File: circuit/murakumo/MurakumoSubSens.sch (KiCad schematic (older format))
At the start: 2 parts

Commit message: hoge
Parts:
- removed U?: S7136, symbol S7136:S7136
- added C35, C36: 0.1u, symbol Device:C
- added D20, D21: LED, symbol Device:LED
- added D22, D23: SIR19-21C/TR8, symbol Device:LED
- added J16, J17: Conn_01x03, symbol Connector_Generic:Conn_01x03
- added R49, R50, R51, R52: R, symbol Device:R
- added R53, R54: 10k, symbol Device:R
- added U6: S7136, symbol S7136:S7136
- gave numbers to parts that had none: 1
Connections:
- net at U5.1 (Cathode): now also D22.1 (K)
- net +5V: now reaches U5.2 (VCC)
- net +5V: now also C35.1, C36.1, J16.3 (Pin_3), J17.3 (Pin_3), R49.1, R50.1, R51.1, R52.1, R53.1, R54.1, U6.2 (VCC)
- net at U5.3 (VOUT): now also D20.1 (K), J16.2 (Pin_2), R53.2
- net GND: now reaches U5.4 (GND)
- net GND: now also C35.2, C36.2, J16.1 (Pin_1), J17.1 (Pin_1), U6.4 (GND)
- new net: D22.2 (A), R51.2
- new net: D20.2 (A), R49.2
- new net: D23.1 (K), U6.1 (Cathode)
- new net: D21.1 (K), J17.2 (Pin_2), R54.2, U6.3 (VOUT)
- new net: D23.2 (A), R52.2
- new net: D21.2 (A), R50.2

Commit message: hoge
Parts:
- removed C35: 0.1u, symbol Device:C
- removed D20, D21: LED, symbol Device:LED
- removed D22: SIR19-21C/TR8, symbol Device:LED
- removed J16: Conn_01x03, symbol Connector_Generic:Conn_01x03
- removed R49, R50, R51: R, symbol Device:R
- removed R53, R54: 10k, symbol Device:R
- removed U5: S7136, symbol S7136:S7136
- added C?: 0.1u, symbol Device:C
- added D?: SIR19-21C/TR8, symbol Device:LED
- added J?: Conn_01x03, symbol Connector_Generic:Conn_01x03
- added R?: 68, symbol Device:R
- added U?: S7136, symbol S7136:S7136
- R52: value R -> 68
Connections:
- net +5V: now also C?.1, J?.3 (Pin_3), R?.1, U?.2 (VCC)
- net GND: now also C?.2, J?.1 (Pin_1), U?.4 (GND)
- new net: D?.1 (K), U?.1 (Cathode)
- new net: J?.2 (Pin_2), U?.3 (VOUT)
- new net: D?.2 (A), R?.2
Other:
- moved on the sheet: C36, J17

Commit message: オシレータ増やした。モータドライバの信号を CPU で読めるようにした。nRST にプルアップ抵抗を接続。まだ CPU の正しいピンに正しい線をつなげることができていない。
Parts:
- gave numbers to parts that had none: 5
- renumbered C36 to C47, D23 to D25, J17 to J20, R52 to R59, U6 to U9
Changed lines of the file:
@@
 $EndDescr
 $Comp
-L S7136:S7136 U6
+L S7136:S7136 U9
 U 1 1 61F63F2D
 P 7000 3450
-F 0 "U6" H 7000 3765 50  0000 C CNN
+F 0 "U9" H 7000 3765 50  0000 C CNN
 F 1 "S7136" H 7000 3674 50  0000 C CNN
 F 2 "" H 7000 3450 50  0001 C CNN
@@
 	7450 3400 7550 3400
 $Comp
-L Device:LED D23
+L Device:LED D25
 U 1 1 61F63F34
 P 7700 3200
-F 0 "D23" V 7739 3082 50  0000 R CNN
+F 0 "D25" V 7739 3082 50  0000 R CNN
 F 1 "SIR19-21C/TR8" V 7648 3082 50  0000 R CNN
 F 2 "" H 7700 3200 50  0001 C CNN
@@
 $EndComp
 $Comp
-L Device:R R52
+L Device:R R59
 U 1 1 61F63F3A
 P 7700 2800
-F 0 "R52" H 7770 2846 50  0000 L CNN
+F 0 "R59" H 7770 2846 50  0000 L CNN
 F 1 "68" H 7770 2755 50  0000 L CNN
 F 2 "" V 7630 2800 50  0001 C CNN
@@
 	7550 2500 7700 2500
 $Comp
-L Connector_Generic:Conn_01x03 J17
+L Connector_Generic:Conn_01x03 J20
 U 1 1 61F63F62
 P 5950 3400
-F 0 "J17" H 5868 3075 50  0000 C CNN
+F 0 "J20" H 5868 3075 50  0000 C CNN
 F 1 "Conn_01x03" H 5868 3166 50  0000 C CNN
 F 2 "" H 5950 3400 50  0001 C CNN
@@
 Connection ~ 6300 2500
 $Comp
-L Device:C C36
+L Device:C C47
 U 1 1 61F63F73
 P 6450 2950
-F 0 "C36" H 6565 2996 50  0000 L CNN
+F 0 "C47" H 6565 2996 50  0000 L CNN
 F 1 "0.1u" H 6565 2905 50  0000 L CNN
 F 2 "" H 6488 2800 50  0001 C CNN
@@
 Connection ~ 6450 2500
 $Comp
-L power:GND #PWR0242
+L power:GND #PWR0164
 U 1 1 61F6B876
 P 6450 3600
-F 0 "#PWR0242" H 6450 3350 50  0001 C CNN
+F 0 "#PWR0164" H 6450 3350 50  0001 C CNN
 F 1 "GND" H 6455 3427 50  0000 C CNN
 F 2 "" H 6450 3600 50  0001 C CNN
@@
 	6450 3600 6450 3500
 $Comp
-L power:PWR_FLAG #FLG0106
-U 1 1 61F6D0AF
-P 6250 4200
-F 0 "#FLG0106" H 6250 4275 50  0001 C CNN
-F 1 "PWR_FLAG" H 6250 4373 50  0000 C CNN
-F 2 "" H 6250 4200 50  0001 C CNN
-F 3 "~" H 6250 4200 50  0001 C CNN
-	1    6250 4200
-	1    0    0    -1
-$EndComp
-$Comp
-L power:GND #PWR0243
-U 1 1 61F6D38D
-P 6250 4450
-F 0 "#PWR0243" H 6250 4200 50  0001 C CNN
-F 1 "GND" H 6255 4277 50  0000 C CNN
-F 2 "" H 6250 4450 50  0001 C CNN
-F 3 "" H 6250 4450 50  0001 C CNN
-	1    6250 4450
-	1    0    0    -1
-$EndComp
-Wire Wire Line
-	6250 4450 6250 4200
-$Comp
-L power:PWR_FLAG #FLG0107
-U 1 1 61F6EBC2
-P 5750 4450
-F 0 "#FLG0107" H 5750 4525 50  0001 C CNN
-F 1 "PWR_FLAG" H 5750 4623 50  0000 C CNN
-F 2 "" H 5750 4450 50  0001 C CNN
-F 3 "~" H 5750 4450 50  0001 C CNN
-	1    5750 4450
-	-1   0    0    1
-$EndComp
-Wire Wire Line
-	5750 4450 5750 4200
-$Comp
-L power:+5V #PWR0240
+L power:+5V #PWR0162
 U 1 1 624AE95B
 P 6300 2400
-F 0 "#PWR0240" H 6300 2250 50  0001 C CNN
+F 0 "#PWR0162" H 6300 2250 50  0001 C CNN
 F 1 "+5V" H 6315 2573 50  0000 C CNN
 F 2 "" H 6300 2400 50  0001 C CNN
@@
 	1    0    0    -1
 $EndComp
-$Comp
-L power:+5V #PWR0244
-U 1 1 624AF64C
-P 5750 4200
-F 0 "#PWR0244" H 5750 4050 50  0001 C CNN
-F 1 "+5V" H 5765 4373 50  0000 C CNN
-F 2 "" H 5750 4200 50  0001 C CNN
-F 3 "" H 5750 4200 50  0001 C CNN
-	1    5750 4200
-	1    0    0    -1
-$EndComp
 Wire Wire Line
 	6450 2500 7550 2500
@@
 	6150 3400 6550 3400
 $Comp
-L S7136:S7136 U?
+L S7136:S7136 U8
 U 1 1 62E812F5
 P 4300 3450
-F 0 "U?" H 4300 3765 50  0000 C CNN
+F 0 "U8" H 4300 3765 50  0000 C CNN
 F 1 "S7136" H 4300 3674 50  0000 C CNN
 F 2 "" H 4300 3450 50  0001 C CNN
@@
 	4750 3400 4850 3400
 $Comp
-L Device:LED D?
+L Device:LED D24
 U 1 1 62E812FC
 P 5000 3200
-F 0 "D?" V 5039 3082 50  0000 R CNN
+F 0 "D24" V 5039 3082 50  0000 R CNN
 F 1 "SIR19-21C/TR8" V 4948 3082 50  0000 R CNN
 F 2 "" H 5000 3200 50  0001 C CNN
@@
 $EndComp
 $Comp
-L Device:R R?
+L Device:R R58
 U 1 1 62E81302
 P 5000 2800
-F 0 "R?" H 5070 2846 50  0000 L CNN
+F 0 "R58" H 5070 2846 50  0000 L CNN
 F 1 "68" H 5070 2755 50  0000 L CNN
 F 2 "" V 4930 2800 50  0001 C CNN
@@
 	4850 2500 5000 2500
 $Comp
-L Connector_Generic:Conn_01x03 J?
+L Connector_Generic:Conn_01x03 J19
 U 1 1 62E8130F
 P 3250 3400
-F 0 "J?" H 3168 3075 50  0000 C CNN
+F 0 "J19" H 3168 3075 50  0000 C CNN
 F 1 "Conn_01x03" H 3168 3166 50  0000 C CNN
 F 2 "" H 3250 3400 50  0001 C CNN
@@
 Connection ~ 3600 2500
 $Comp
-L Device:C C?
+L Device:C C46
 U 1 1 62E8131A
 P 3750 2950
-F 0 "C?" H 3865 2996 50  0000 L CNN
+F 0 "C46" H 3865 2996 50  0000 L CNN
 F 1 "0.1u" H 3865 2905 50  0000 L CNN
 F 2 "" H 3788 2800 50  0001 C CNN
@@
 Connection ~ 3750 2500
 $Comp
-L power:GND #PWR?
+L power:GND #PWR0163
 U 1 1 62E81326
 P 3750 3600
-F 0 "#PWR?" H 3750 3350 50  0001 C CNN
+F 0 "#PWR0163" H 3750 3350 50  0001 C CNN
 F 1 "GND" H 3755 3427 50  0000 C CNN
 F 2 "" H 3750 3600 50  0001 C CNN
@@
 	3750 3600 3750 3500
 $Comp
-L power:+5V #PWR?
+L power:+5V #PWR0161
 U 1 1 62E8132D
 P 3600 2400
-F 0 "#PWR?" H 3600 2250 50  0001 C CNN
+F 0 "#PWR0161" H 3600 2250 50  0001 C CNN
 F 1 "+5V" H 3615 2573 50  0000 C CNN
 F 2 "" H 3600 2400 50  0001 C CNN

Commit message: 次はフットプリントの関連付け
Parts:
- D13: renamed from D24; footprint (none) -> Diode_SMD:D_0603_1608Metric
- D14: renamed from D25; footprint (none) -> Diode_SMD:D_0603_1608Metric
- J10: renamed from J20; value Conn_01x03 -> CPU_GPIO
- J9: renamed from J19; value Conn_01x03 -> CPU_GPIO
- U6: renamed from U9; footprint (none) -> original:TSSOP_16-Pin
- renumbered C46 to C23, C47 to C24, R58 to R30, R59 to R31, U8 to U5
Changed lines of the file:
@@
 $Descr A4 11693 8268
 encoding utf-8
-Sheet 4 4
+Sheet 4 5
 Title "Murakumo_Side_Sensor_Circuit"
 Date ""
@@
 $EndDescr
 $Comp
-L S7136:S7136 U9
+L S7136:S7136 U6
 U 1 1 61F63F2D
 P 7000 3450
-F 0 "U9" H 7000 3765 50  0000 C CNN
+F 0 "U6" H 7000 3765 50  0000 C CNN
 F 1 "S7136" H 7000 3674 50  0000 C CNN
-F 2 "" H 7000 3450 50  0001 C CNN
+F 2 "original:TSSOP_16-Pin" H 7000 3450 50  0001 C CNN
 F 3 "https://www.hamamatsu.com/resources/pdf/ssd/s4282-51_etc_kpic1002j.pdf" H 7000 3450 50  0001 C CNN
 	1    7000 3450
@@
 	7450 3400 7550 3400
 $Comp
-L Device:LED D25
+L Device:LED D14
 U 1 1 61F63F34
 P 7700 3200
-F 0 "D25" V 7739 3082 50  0000 R CNN
+F 0 "D14" V 7739 3082 50  0000 R CNN
 F 1 "SIR19-21C/TR8" V 7648 3082 50  0000 R CNN
-F 2 "" H 7700 3200 50  0001 C CNN
+F 2 "Diode_SMD:D_0603_1608Metric" H 7700 3200 50  0001 C CNN
 F 3 "~" H 7700 3200 50  0001 C CNN
 	1    7700 3200
@@
 $EndComp
 $Comp
-L Device:R R59
+L Device:R R31
 U 1 1 61F63F3A
 P 7700 2800
-F 0 "R59" H 7770 2846 50  0000 L CNN
+F 0 "R31" H 7770 2846 50  0000 L CNN
 F 1 "68" H 7770 2755 50  0000 L CNN
 F 2 "" V 7630 2800 50  0001 C CNN
@@
 	7550 2500 7700 2500
 $Comp
-L Connector_Generic:Conn_01x03 J20
+L Connector_Generic:Conn_01x03 J10
 U 1 1 61F63F62
 P 5950 3400
-F 0 "J20" H 5868 3075 50  0000 C CNN
-F 1 "Conn_01x03" H 5868 3166 50  0000 C CNN
+F 0 "J10" H 5868 3075 50  0000 C CNN
+F 1 "CPU_GPIO" H 5868 3166 50  0000 C CNN
 F 2 "" H 5950 3400 50  0001 C CNN
 F 3 "~" H 5950 3400 50  0001 C CNN
@@
 Connection ~ 6300 2500
 $Comp
-L Device:C C47
+L Device:C C24
 U 1 1 61F63F73
 P 6450 2950
-F 0 "C47" H 6565 2996 50  0000 L CNN
+F 0 "C24" H 6565 2996 50  0000 L CNN
 F 1 "0.1u" H 6565 2905 50  0000 L CNN
 F 2 "" H 6488 2800 50  0001 C CNN
@@
 Connection ~ 6450 2500
 $Comp
-L power:GND #PWR0164
+L power:GND #PWR073
 U 1 1 61F6B876
 P 6450 3600
-F 0 "#PWR0164" H 6450 3350 50  0001 C CNN
+F 0 "#PWR073" H 6450 3350 50  0001 C CNN
 F 1 "GND" H 6455 3427 50  0000 C CNN
 F 2 "" H 6450 3600 50  0001 C CNN
@@
 	6450 3600 6450 3500
 $Comp
-L power:+5V #PWR0162
+L power:+5V #PWR071
 U 1 1 624AE95B
 P 6300 2400
-F 0 "#PWR0162" H 6300 2250 50  0001 C CNN
+F 0 "#PWR071" H 6300 2250 50  0001 C CNN
 F 1 "+5V" H 6315 2573 50  0000 C CNN
 F 2 "" H 6300 2400 50  0001 C CNN
@@
 	6150 3400 6550 3400
 $Comp
-L S7136:S7136 U8
+L S7136:S7136 U5
 U 1 1 62E812F5
 P 4300 3450
-F 0 "U8" H 4300 3765 50  0000 C CNN
+F 0 "U5" H 4300 3765 50  0000 C CNN
 F 1 "S7136" H 4300 3674 50  0000 C CNN
 F 2 "" H 4300 3450 50  0001 C CNN
@@
 	4750 3400 4850 3400
 $Comp
-L Device:LED D24
+L Device:LED D13
 U 1 1 62E812FC
 P 5000 3200
-F 0 "D24" V 5039 3082 50  0000 R CNN
+F 0 "D13" V 5039 3082 50  0000 R CNN
 F 1 "SIR19-21C/TR8" V 4948 3082 50  0000 R CNN
-F 2 "" H 5000 3200 50  0001 C CNN
+F 2 "Diode_SMD:D_0603_1608Metric" H 5000 3200 50  0001 C CNN
 F 3 "~" H 5000 3200 50  0001 C CNN
 	1    5000 3200
@@
 $EndComp
 $Comp
-L Device:R R58
+L Device:R R30
 U 1 1 62E81302
 P 5000 2800
-F 0 "R58" H 5070 2846 50  0000 L CNN
+F 0 "R30" H 5070 2846 50  0000 L CNN
 F 1 "68" H 5070 2755 50  0000 L CNN
 F 2 "" V 4930 2800 50  0001 C CNN
@@
 	4850 2500 5000 2500
 $Comp
-L Connector_Generic:Conn_01x03 J19
+L Connector_Generic:Conn_01x03 J9
 U 1 1 62E8130F
 P 3250 3400
-F 0 "J19" H 3168 3075 50  0000 C CNN
-F 1 "Conn_01x03" H 3168 3166 50  0000 C CNN
+F 0 "J9" H 3168 3075 50  0000 C CNN
+F 1 "CPU_GPIO" H 3168 3166 50  0000 C CNN
 F 2 "" H 3250 3400 50  0001 C CNN
 F 3 "~" H 3250 3400 50  0001 C CNN
@@
 Connection ~ 3600 2500
 $Comp
-L Device:C C46
+L Device:C C23
 U 1 1 62E8131A
 P 3750 2950
-F 0 "C46" H 3865 2996 50  0000 L CNN
+F 0 "C23" H 3865 2996 50  0000 L CNN
 F 1 "0.1u" H 3865 2905 50  0000 L CNN
 F 2 "" H 3788 2800 50  0001 C CNN
@@
 Connection ~ 3750 2500
 $Comp
-L power:GND #PWR0163
+L power:GND #PWR072
 U 1 1 62E81326
 P 3750 3600
-F 0 "#PWR0163" H 3750 3350 50  0001 C CNN
+F 0 "#PWR072" H 3750 3350 50  0001 C CNN
 F 1 "GND" H 3755 3427 50  0000 C CNN
 F 2 "" H 3750 3600 50  0001 C CNN
@@
 	3750 3600 3750 3500
 $Comp
-L power:+5V #PWR0161
+L power:+5V #PWR070
 U 1 1 62E8132D
 P 3600 2400
-F 0 "#PWR0161" H 3600 2250 50  0001 C CNN
+F 0 "#PWR070" H 3600 2250 50  0001 C CNN
 F 1 "+5V" H 3615 2573 50  0000 C CNN
 F 2 "" H 3600 2400 50  0001 C CNN

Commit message: あとちょっとでフットプリントの関連付けが終わる
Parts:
- C23, C24: footprint (none) -> Capacitor_SMD:C_0603_1608Metric
- J10, J9: value CPU_GPIO -> SH3
- R30, R31: footprint (none) -> Resistor_SMD:R_0603_1608Metric
- U5: footprint (none) -> sens:S7136
- U6: footprint original:TSSOP_16-Pin -> sens:S7136
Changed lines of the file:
@@
 F 0 "U6" H 7000 3765 50  0000 C CNN
 F 1 "S7136" H 7000 3674 50  0000 C CNN
-F 2 "original:TSSOP_16-Pin" H 7000 3450 50  0001 C CNN
+F 2 "sens:S7136" H 7000 3450 50  0001 C CNN
 F 3 "https://www.hamamatsu.com/resources/pdf/ssd/s4282-51_etc_kpic1002j.pdf" H 7000 3450 50  0001 C CNN
 	1    7000 3450
@@
 F 0 "R31" H 7770 2846 50  0000 L CNN
 F 1 "68" H 7770 2755 50  0000 L CNN
-F 2 "" V 7630 2800 50  0001 C CNN
+F 2 "Resistor_SMD:R_0603_1608Metric" V 7630 2800 50  0001 C CNN
 F 3 "~" H 7700 2800 50  0001 C CNN
 	1    7700 2800
@@
 P 5950 3400
 F 0 "J10" H 5868 3075 50  0000 C CNN
-F 1 "CPU_GPIO" H 5868 3166 50  0000 C CNN
+F 1 "SH3" H 5868 3166 50  0000 C CNN
 F 2 "" H 5950 3400 50  0001 C CNN
 F 3 "~" H 5950 3400 50  0001 C CNN
@@
 F 0 "C24" H 6565 2996 50  0000 L CNN
 F 1 "0.1u" H 6565 2905 50  0000 L CNN
-F 2 "" H 6488 2800 50  0001 C CNN
+F 2 "Capacitor_SMD:C_0603_1608Metric" H 6488 2800 50  0001 C CNN
 F 3 "~" H 6450 2950 50  0001 C CNN
 	1    6450 2950
@@
 F 0 "U5" H 4300 3765 50  0000 C CNN
 F 1 "S7136" H 4300 3674 50  0000 C CNN
-F 2 "" H 4300 3450 50  0001 C CNN
+F 2 "sens:S7136" H 4300 3450 50  0001 C CNN
 F 3 "https://www.hamamatsu.com/resources/pdf/ssd/s4282-51_etc_kpic1002j.pdf" H 4300 3450 50  0001 C CNN
 	1    4300 3450
@@
 F 0 "R30" H 5070 2846 50  0000 L CNN
 F 1 "68" H 5070 2755 50  0000 L CNN
-F 2 "" V 4930 2800 50  0001 C CNN
+F 2 "Resistor_SMD:R_0603_1608Metric" V 4930 2800 50  0001 C CNN
 F 3 "~" H 5000 2800 50  0001 C CNN
 	1    5000 2800
@@
 P 3250 3400
 F 0 "J9" H 3168 3075 50  0000 C CNN
-F 1 "CPU_GPIO" H 3168 3166 50  0000 C CNN
+F 1 "SH3" H 3168 3166 50  0000 C CNN
 F 2 "" H 3250 3400 50  0001 C CNN
 F 3 "~" H 3250 3400 50  0001 C CNN
@@
 F 0 "C23" H 3865 2996 50  0000 L CNN
 F 1 "0.1u" H 3865 2905 50  0000 L CNN
-F 2 "" H 3788 2800 50  0001 C CNN
+F 2 "Capacitor_SMD:C_0603_1608Metric" H 3788 2800 50  0001 C CNN
 F 3 "~" H 3750 2950 50  0001 C CNN
 	1    3750 2950

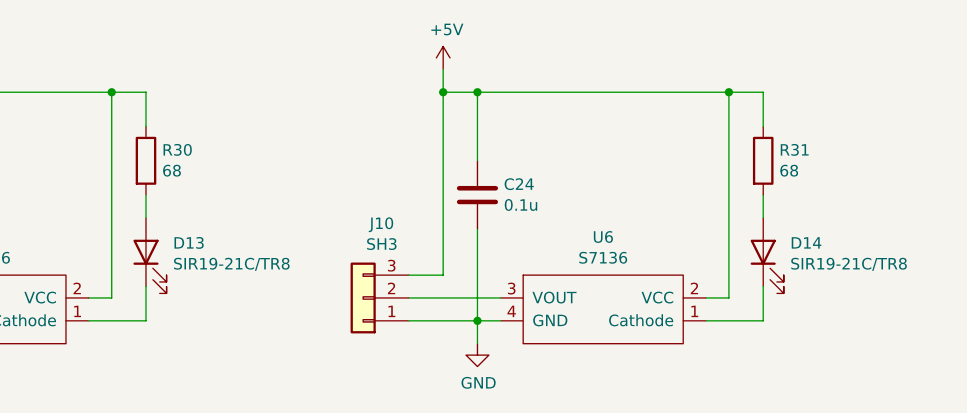
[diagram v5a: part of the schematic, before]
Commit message: 回路図とフットプリントの関連付けが終わった
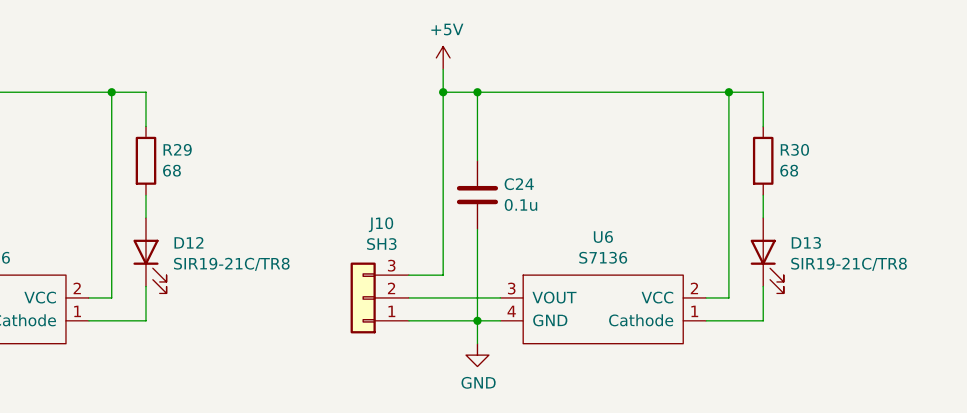
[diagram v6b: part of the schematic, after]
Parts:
- J10, J9: footprint (none) -> SH:SH_01x03
- renumbered D13 to D12, D14 to D13, R30 to R29, R31 to R30
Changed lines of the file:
@@
 	7450 3400 7550 3400
 $Comp
-L Device:LED D14
+L Device:LED D13
 U 1 1 61F63F34
 P 7700 3200
-F 0 "D14" V 7739 3082 50  0000 R CNN
+F 0 "D13" V 7739 3082 50  0000 R CNN
 F 1 "SIR19-21C/TR8" V 7648 3082 50  0000 R CNN
 F 2 "Diode_SMD:D_0603_1608Metric" H 7700 3200 50  0001 C CNN
@@
 $EndComp
 $Comp
-L Device:R R31
+L Device:R R30
 U 1 1 61F63F3A
 P 7700 2800
-F 0 "R31" H 7770 2846 50  0000 L CNN
+F 0 "R30" H 7770 2846 50  0000 L CNN
 F 1 "68" H 7770 2755 50  0000 L CNN
 F 2 "Resistor_SMD:R_0603_1608Metric" V 7630 2800 50  0001 C CNN
@@
 F 0 "J10" H 5868 3075 50  0000 C CNN
 F 1 "SH3" H 5868 3166 50  0000 C CNN
-F 2 "" H 5950 3400 50  0001 C CNN
+F 2 "SH:SH_01x03" H 5950 3400 50  0001 C CNN
 F 3 "~" H 5950 3400 50  0001 C CNN
 	1    5950 3400
@@
 Connection ~ 6450 2500
 $Comp
-L power:GND #PWR073
+L power:GND #PWR072
 U 1 1 61F6B876
 P 6450 3600
-F 0 "#PWR073" H 6450 3350 50  0001 C CNN
+F 0 "#PWR072" H 6450 3350 50  0001 C CNN
 F 1 "GND" H 6455 3427 50  0000 C CNN
 F 2 "" H 6450 3600 50  0001 C CNN
@@
 	6450 3600 6450 3500
 $Comp
-L power:+5V #PWR071
+L power:+5V #PWR070
 U 1 1 624AE95B
 P 6300 2400
-F 0 "#PWR071" H 6300 2250 50  0001 C CNN
+F 0 "#PWR070" H 6300 2250 50  0001 C CNN
 F 1 "+5V" H 6315 2573 50  0000 C CNN
 F 2 "" H 6300 2400 50  0001 C CNN
@@
 	4750 3400 4850 3400
 $Comp
-L Device:LED D13
+L Device:LED D12
 U 1 1 62E812FC
 P 5000 3200
-F 0 "D13" V 5039 3082 50  0000 R CNN
+F 0 "D12" V 5039 3082 50  0000 R CNN
 F 1 "SIR19-21C/TR8" V 4948 3082 50  0000 R CNN
 F 2 "Diode_SMD:D_0603_1608Metric" H 5000 3200 50  0001 C CNN
@@
 $EndComp
 $Comp
-L Device:R R30
+L Device:R R29
 U 1 1 62E81302
 P 5000 2800
-F 0 "R30" H 5070 2846 50  0000 L CNN
+F 0 "R29" H 5070 2846 50  0000 L CNN
 F 1 "68" H 5070 2755 50  0000 L CNN
 F 2 "Resistor_SMD:R_0603_1608Metric" V 4930 2800 50  0001 C CNN
@@
 F 0 "J9" H 3168 3075 50  0000 C CNN
 F 1 "SH3" H 3168 3166 50  0000 C CNN
-F 2 "" H 3250 3400 50  0001 C CNN
+F 2 "SH:SH_01x03" H 3250 3400 50  0001 C CNN
 F 3 "~" H 3250 3400 50  0001 C CNN
 	1    3250 3400
@@
 Connection ~ 3750 2500
 $Comp
-L power:GND #PWR072
+L power:GND #PWR071
 U 1 1 62E81326
 P 3750 3600
-F 0 "#PWR072" H 3750 3350 50  0001 C CNN
+F 0 "#PWR071" H 3750 3350 50  0001 C CNN
 F 1 "GND" H 3755 3427 50  0000 C CNN
 F 2 "" H 3750 3600 50  0001 C CNN
@@
 	3750 3600 3750 3500
 $Comp
-L power:+5V #PWR070
+L power:+5V #PWR069
 U 1 1 62E8132D
 P 3600 2400
-F 0 "#PWR070" H 3600 2250 50  0001 C CNN
+F 0 "#PWR069" H 3600 2250 50  0001 C CNN
 F 1 "+5V" H 3615 2573 50  0000 C CNN
 F 2 "" H 3600 2400 50  0001 C CNN
